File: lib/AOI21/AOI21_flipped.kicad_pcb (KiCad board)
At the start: 2 copper layers, 6 parts

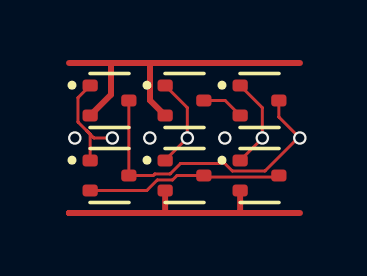
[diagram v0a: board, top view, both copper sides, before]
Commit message: High-density layout with pitch of 1.1mm, which gains 23% !!
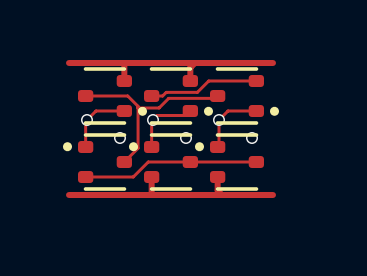
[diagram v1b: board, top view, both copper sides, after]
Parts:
- moved P3 0.87 mm to (5.50, 3.30)
- moved N3 0.76 mm to (5.50, 1.10), turned to 180 degrees
- moved P2 0.64 mm to (3.30, 3.30)
- moved N2 0.47 mm to (3.30, 1.10), turned to 180 degrees
- moved P1 0.47 mm to (1.10, 3.30)
- moved N1 0.21 mm to (1.10, 1.10), turned to 180 degrees
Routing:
- net Y: track 10.5 -> 6.75 mm, vias 1 -> 0
- net GND: track 11.7 -> 8.09 mm
- net intB: track 1.42 -> 3.70 mm
- net A: track 3.79 -> 2.29 mm
- net VDD: track 9.23 -> 8.08 mm
- net B2: track 3.11 -> 2.29 mm
- net intP: track 6.54 -> 5.90 mm
- net B1: track 3.11 -> 2.50 mm

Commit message: All cells now use 1mm*4mm grid rather than 1.1mm*4.4mm
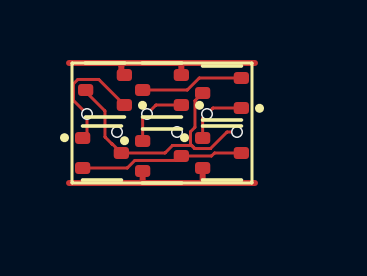
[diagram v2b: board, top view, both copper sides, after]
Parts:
- moved P3 0.58 mm to (5.00, 3.00)
- moved N3 0.51 mm to (5.00, 1.00)
- moved N2 0.36 mm to (3.00, 0.90)
- moved P2 0.36 mm to (3.00, 3.10)
- moved P1 0.32 mm to (1.00, 3.00)
- moved N1 0.20 mm to (1.10, 0.90)
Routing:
- net Y: track 6.75 -> 8.93 mm, vias 0 -> 1
- net A: track 2.29 -> 4.16 mm
- net GND: track 8.09 -> 7.15 mm
- net VDD: track 8.08 -> 7.14 mm
- net (no net): vias 3 -> 2

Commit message: Make the pads of my SOT523 footprint very slightly smaller, which is enough to route all the cells and leave the mosfets exactly on the grid
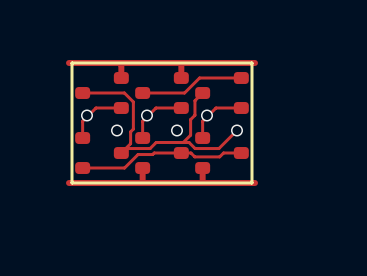
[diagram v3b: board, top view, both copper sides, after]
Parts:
- N1, N2, N3, P1, P2, P3: footprint Package_TO_SOT_SMD:SOT-523 -> RV523:SOT523
- moved N1 0.14 mm to (1.00, 1.00)
- moved P2 0.10 mm to (3.00, 3.00)
- moved N2 0.10 mm to (3.00, 1.00)
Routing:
- net A: track 4.16 -> 2.03 mm
- net Y: track 8.93 -> 10.1 mm

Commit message: Propagate MOSFET values to the cells' PCBs
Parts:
- N1, N2, N3: value (none) -> NMOS
- P1, P2, P3: value (none) -> PMOS
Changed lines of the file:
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@@
 			)
 		)
-		(property "Value" ""
+		(property "Value" "PMOS"
 			(at 0 0 0)
 			(layer "F.Fab")
@@
 			)
 		)
-		(property "Value" ""
+		(property "Value" "NMOS"
 			(at 0 0 180)
 			(layer "F.Fab")
@@
 			)
 		)
-		(property "Value" ""
+		(property "Value" "PMOS"
 			(at 0 0 0)
 			(layer "F.Fab")
@@
 			)
 		)
-		(property "Value" ""
+		(property "Value" "NMOS"
 			(at 0 0 180)
 			(layer "F.Fab")
@@
 			)
 		)
-		(property "Value" ""
+		(property "Value" "NMOS"
 			(at 0 0 180)
 			(layer "F.Fab")
@@
 			)
 		)
-		(property "Value" ""
+		(property "Value" "PMOS"
 			(at 0 0 0)
 			(layer "F.Fab")

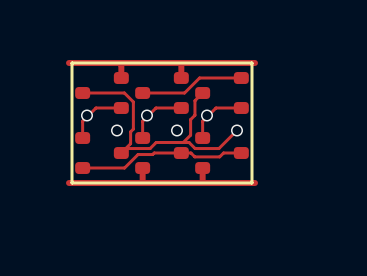
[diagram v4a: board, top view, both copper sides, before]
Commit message: Update AOI21 layout
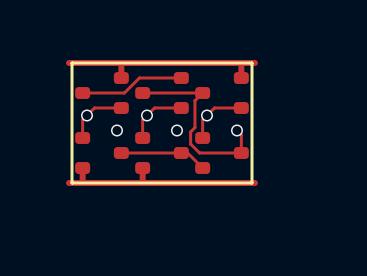
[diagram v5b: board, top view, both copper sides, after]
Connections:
- net A renamed A1
- N1 pad 3: Y -> sndA1
- N2 pad 1: B1 -> A2
- N2 pad 2: GND -> sndA1
- N2 pad 3: intB -> Y
- N3 pad 1: B2 -> B1
- N3 pad 2: intB -> GND
- P1 pad 2: intP -> VDD
- P1 pad 3: Y -> pndA
- P2 pad 1: B1 -> A2
- P2 pad 3: intP -> pndA
- P3 pad 1: B2 -> B1
- P3 pad 2: VDD -> pndA
- P3 pad 3: intP -> Y
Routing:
- net intP: track 5.60 -> 0.00 mm
- net Y: track 10.1 -> 6.49 mm
- net sndA1: track 0.00 -> 3.50 mm
- net intB: track 3.50 -> 0.00 mm
- net pndA: track 0.00 -> 2.92 mm
- net A2: track 0.00 -> 2.06 mm, vias 0 -> 1
- net B2: track 2.03 -> 0.00 mm, vias 1 -> 0
